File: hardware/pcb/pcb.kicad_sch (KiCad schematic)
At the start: 0 parts

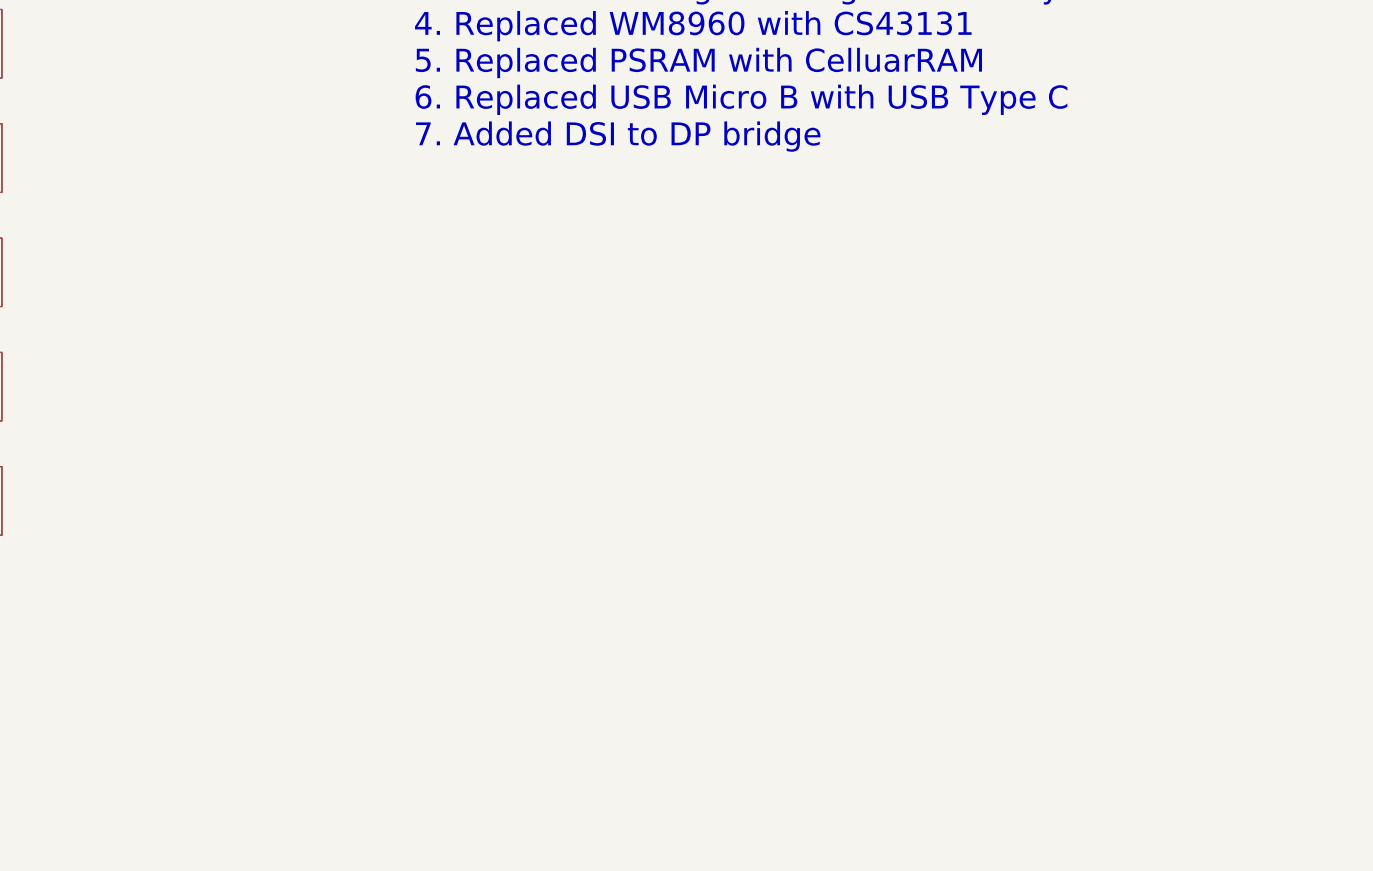
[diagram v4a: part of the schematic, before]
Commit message: - pcb: r0p4, update to KiCAD 6.0
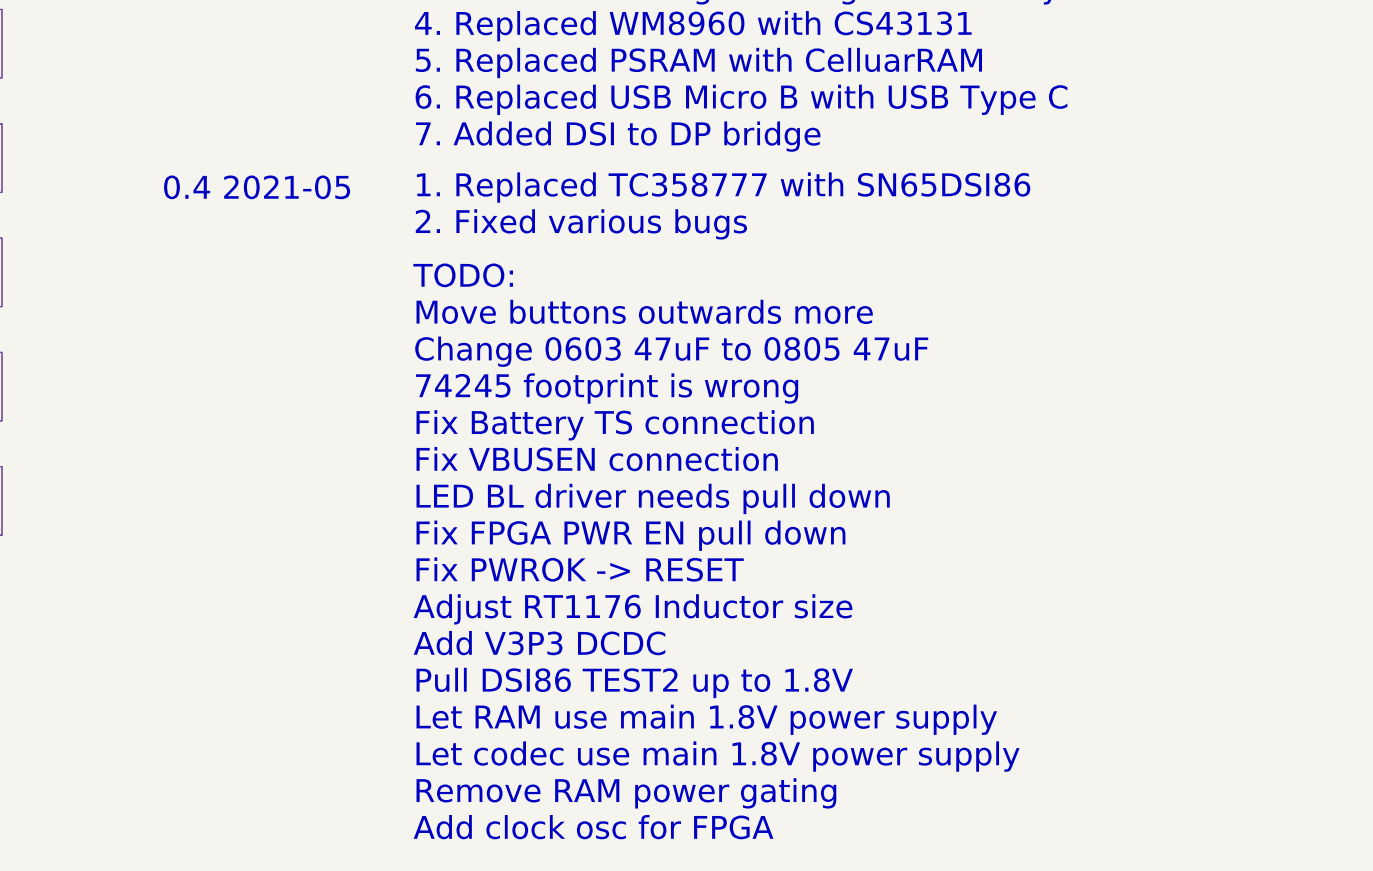
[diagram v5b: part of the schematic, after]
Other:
- note added: "0.4 2021-05"
- note added: "1. Replaced TC358777 with SN65DSI86 2. Fixed various bugs"
- note added: "TODO: Move buttons outwards more Change 0603 47uF to 0805 47uF 74245 footprint is wrong Fix Battery TS connection Fix VBUSEN connection LED BL driver needs pull down Fix FPGA PWR EN pull down Fix PWROK -> RESET Adjust RT1176 Inductor size Add V3P3 DCDC Pull DSI86 TEST2 up to 1.8V Let RAM use main 1.8V power supply Let codec use main 1.8V power supply Remove RAM power gating Add clock osc for FPGA"
